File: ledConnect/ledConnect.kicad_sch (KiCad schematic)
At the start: 15 parts, among them U1 MT30-M, U2 TPS565208DDCR

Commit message: add layout
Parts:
- added Q1: AO4407A, easyeda2kicad:SOIC-8_L4.9-W3.9-P1.27-LS6.0-BL, symbol easyeda2kicad:AO4407A
- added R1: 100R, symbol Device:R
- added R2: 1M, symbol Device:R
- added SW1: SS-12M11G5, easyeda2kicad:SW-TH_XKB_SS-12M11XX, symbol easyeda2kicad:SS-12M11G5
- added TP4: LED_VDC, TestPoint:TestPoint_Pad_2.5x2.5mm, symbol Connector:TestPoint
- added TP5: LED_DATA, TestPoint:TestPoint_Pad_2.5x2.5mm, symbol Connector:TestPoint
- added TP6: LED_GND, TestPoint:TestPoint_Pad_2.5x2.5mm, symbol Connector:TestPoint
- TP1, TP2, TP3: footprint (none) -> TestPoint:TestPoint_Pad_2.5x2.5mm
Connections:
- net +12V: now also U1.3, Q1.5 (D), Q1.6 (D), Q1.7 (D), Q1.8 (D), R1.1; no longer C2.1, C3.1, C6.1, U2.3 (VIN), U2.5 (EN)
- net GND: now also TP1.1, U1.1, R2.2, TP6.1
- net LED_DATA: now also TP2.1, U1.2, TP5.1
- net VDC: now also TP3.1, SW1.3, TP4.1
- new net: Q1.4 (G), R1.2, R2.1
- new net: Q1.1 (S), Q1.2 (S), Q1.3 (S), SW1.1
- new net EN: C2.1, C3.1, C6.1, SW1.2, U2.3 (VIN), U2.5 (EN)
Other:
- note added: "reverse polarity protection"
- note added: "skip buck converter, if ledsignal is 5v anyway, or if the leds need 12v"
- moved on the sheet: C1, C2, C3, C4, C5, C6, C7, L1, Rfbb, Rfbt, TP1, TP2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

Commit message: next board
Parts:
- C2, C5, C6, C7: footprint (none) -> Capacitor_SMD:C_0805_2012Metric_Pad1.18x1.45mm_HandSolder
- C3, C4: footprint (none) -> Capacitor_SMD:C_0603_1608Metric_Pad1.08x0.95mm_HandSolder
- R1, R2: footprint (none) -> Resistor_SMD:R_0603_1608Metric_Pad0.98x0.95mm_HandSolder
- Rfbb1: renamed from Rfbb; footprint (none) -> Resistor_SMD:R_0603_1608Metric_Pad0.98x0.95mm_HandSolder
- Rfbt1: renamed from Rfbt; footprint (none) -> Resistor_SMD:R_0603_1608Metric_Pad0.98x0.95mm_HandSolder
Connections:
- net EN: now also SW1.1; no longer SW1.2
- net at Q1.1 (S), Q1.2 (S), Q1.3 (S): now also SW1.2; no longer SW1.1
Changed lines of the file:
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@@
 	(text "skip buck converter, \nif ledsignal is 5v anyway, \nor if the leds need 12v"
 		(exclude_from_sim no)
-		(at 108.458 59.69 0)
+		(at 113.03 52.832 0)
 		(effects
 			(font
@@
 	)
 	(junction
+		(at 119.38 73.66)
+		(diameter 0)
+		(color 0 0 0 0)
+	)
+	(junction
 		(at 171.45 81.28)
 		(diameter 0)
@@
 	)
 	(junction
-		(at 119.38 73.66)
-		(diameter 0)
-		(color 0 0 0 0)
-	)
-	(junction
 		(at 222.25 81.28)
 		(diameter 0)
@@
 	(wire
 		(pts
-			(xy 104.14 69.85) (xy 100.33 69.85)
-		)
-		(stroke
-			(width 0)
-			(type default)
-		)
-	)
-	(wire
-		(pts
 			(xy 170.18 129.54) (xy 168.91 129.54)
 		)
@@
 	(wire
 		(pts
-			(xy 95.25 69.85) (xy 95.25 71.12)
-		)
-		(stroke
-			(width 0)
-			(type default)
-		)
-	)
-	(wire
-		(pts
 			(xy 77.47 78.74) (xy 77.47 82.55)
 		)
@@
 	(wire
 		(pts
-			(xy 97.79 73.66) (xy 119.38 73.66)
-		)
-		(stroke
-			(width 0)
-			(type default)
-		)
-	)
-	(wire
-		(pts
 			(xy 119.38 81.28) (xy 132.08 81.28)
 		)
@@
 	(wire
 		(pts
-			(xy 95.25 71.12) (xy 85.09 71.12)
-		)
-		(stroke
-			(width 0)
-			(type default)
-		)
-	)
-	(wire
-		(pts
-			(xy 97.79 69.85) (xy 97.79 73.66)
+			(xy 85.09 71.12) (xy 97.79 71.12)
 		)
 		(stroke
@@
 	(wire
 		(pts
+			(xy 95.25 73.66) (xy 119.38 73.66)
+		)
+		(stroke
+			(width 0)
+			(type default)
+		)
+	)
+	(wire
+		(pts
 			(xy 204.47 74.93) (xy 204.47 81.28)
 		)
@@
 	(wire
 		(pts
+			(xy 95.25 69.85) (xy 95.25 73.66)
+		)
+		(stroke
+			(width 0)
+			(type default)
+		)
+	)
+	(wire
+		(pts
 			(xy 184.15 57.15) (xy 181.61 57.15)
 		)
@@
 		(pts
 			(xy 62.23 73.66) (xy 66.04 73.66)
+		)
+		(stroke
+			(width 0)
+			(type default)
+		)
+	)
+	(wire
+		(pts
+			(xy 97.79 71.12) (xy 97.79 69.85)
 		)
 		(stroke
@@
 			)
 		)
-		(property "Footprint" ""
+		(property "Footprint" "Resistor_SMD:R_0603_1608Metric_Pad0.98x0.95mm_HandSolder"
 			(at 64.262 87.63 90)
 			(effects
@@
 			)
 		)
-		(property "Footprint" ""
+		(property "Footprint" "Capacitor_SMD:C_0805_2012Metric_Pad1.18x1.45mm_HandSolder"
 			(at 235.9152 72.39 0)
 			(effects
@@
 			)
 		)
-		(property "Footprint" ""
+		(property "Footprint" "Capacitor_SMD:C_0805_2012Metric_Pad1.18x1.45mm_HandSolder"
 			(at 120.3452 81.28 0)
 			(effects
@@
 			)
 		)
-		(property "Footprint" ""
+		(property "Footprint" "Capacitor_SMD:C_0805_2012Metric_Pad1.18x1.45mm_HandSolder"
 			(at 223.2152 72.39 0)
 			(effects
@@
 			)
 		)
-		(property "Footprint" ""
+		(property "Footprint" "Capacitor_SMD:C_0603_1608Metric_Pad1.08x0.95mm_HandSolder"
 			(at 182.5752 64.77 0)
 			(effects
@@
 			)
 		)
-		(property "Footprint" ""
+		(property "Footprint" "Capacitor_SMD:C_0805_2012Metric_Pad1.18x1.45mm_HandSolder"
 			(at 133.0452 81.28 0)
 			(effects
@@
 	(symbol
 		(lib_id "power:VDC")
-		(at 104.14 69.85 270)
+		(at 100.33 69.85 270)
 		(unit 1)
 		(exclude_from_sim no)
@@
 		(fields_autoplaced yes)
 		(property "Reference" "#PWR012"
+			(at 96.52 69.85 0)
+			(effects
+				(font
+					(size 1.27 1.27)
+				)
+				(hide yes)
+			)
+		)
+		(property "Value" "VDC"
+			(at 104.14 69.8499 90)
+			(effects
+				(font
+					(size 1.27 1.27)
+				)
+				(justify left)
+			)
+		)
+		(property "Footprint" ""
 			(at 100.33 69.85 0)
 			(effects
@@
 			)
 		)
-		(property "Value" "VDC"
-			(at 107.95 69.8499 90)
-			(effects
-				(font
-					(size 1.27 1.27)
-				)
-				(justify left)
-			)
-		)
-		(property "Footprint" ""
-			(at 104.14 69.85 0)
-			(effects
-				(font
-					(size 1.27 1.27)
-				)
-				(hide yes)
-			)
-		)
 		(property "Datasheet" ""
-			(at 104.14 69.85 0)
+			(at 100.33 69.85 0)
 			(effects
 				(font
@@
 		)
 		(property "Description" "Power symbol creates a global label with name \"VDC\""
-			(at 104.14 69.85 0)
+			(at 100.33 69.85 0)
 			(effects
 				(font
@@
 			)
 		)
-		(property "Footprint" ""
+		(property "Footprint" "Resistor_SMD:R_0603_1608Metric_Pad0.98x0.95mm_HandSolder"
 			(at 64.262 77.47 90)
 			(effects
@@
 			)
 		)
-		(property "Footprint" ""
+		(property "Footprint" "Capacitor_SMD:C_0603_1608Metric_Pad1.08x0.95mm_HandSolder"
 			(at 145.7452 81.28 0)
 			(effects
@@
 		(dnp no)
 		(fields_autoplaced yes)
-		(property "Reference" "Rfbb"
+		(property "Reference" "Rfbb1"
 			(at 207.01 69.8499 0)
 			(effects
@@
 			)
 		)
-		(property "Footprint" ""
+		(property "Footprint" "Resistor_SMD:R_0603_1608Metric_Pad0.98x0.95mm_HandSolder"
 			(at 202.692 71.12 90)
 			(effects
@@
 			(project "ledConnect"
 				(path "/98174448-9966-40ca-80fa-f976aec9577e"
-					(reference "Rfbb")
+					(reference "Rfbb1")
 					(unit 1)
 				)
@@
 		(dnp no)
 		(fields_autoplaced yes)
-		(property "Reference" "Rfbt"
+		(property "Reference" "Rfbt1"
 			(at 207.01 59.6899 0)
 			(effects
@@
 			)
 		)
-		(property "Footprint" ""
+		(property "Footprint" "Resistor_SMD:R_0603_1608Metric_Pad0.98x0.95mm_HandSolder"
 			(at 202.692 60.96 90)
 			(effects
@@
 			(project ""
 				(path "/98174448-9966-40ca-80fa-f976aec9577e"
-					(reference "Rfbt")
-					(unit 1)
-				)
+					(reference "Rfbt1")
+					(unit 1)
+				)

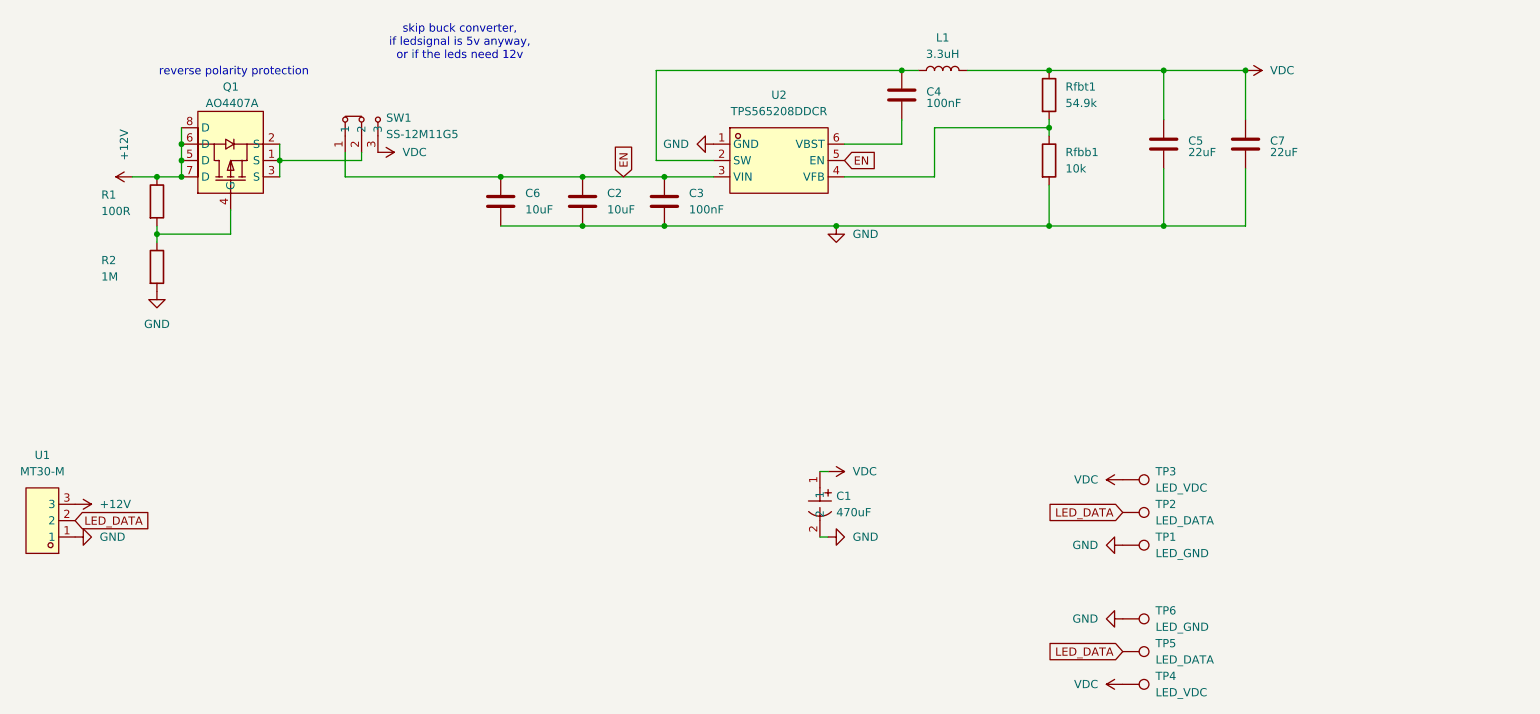
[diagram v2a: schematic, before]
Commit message: via stiching fehlt noch
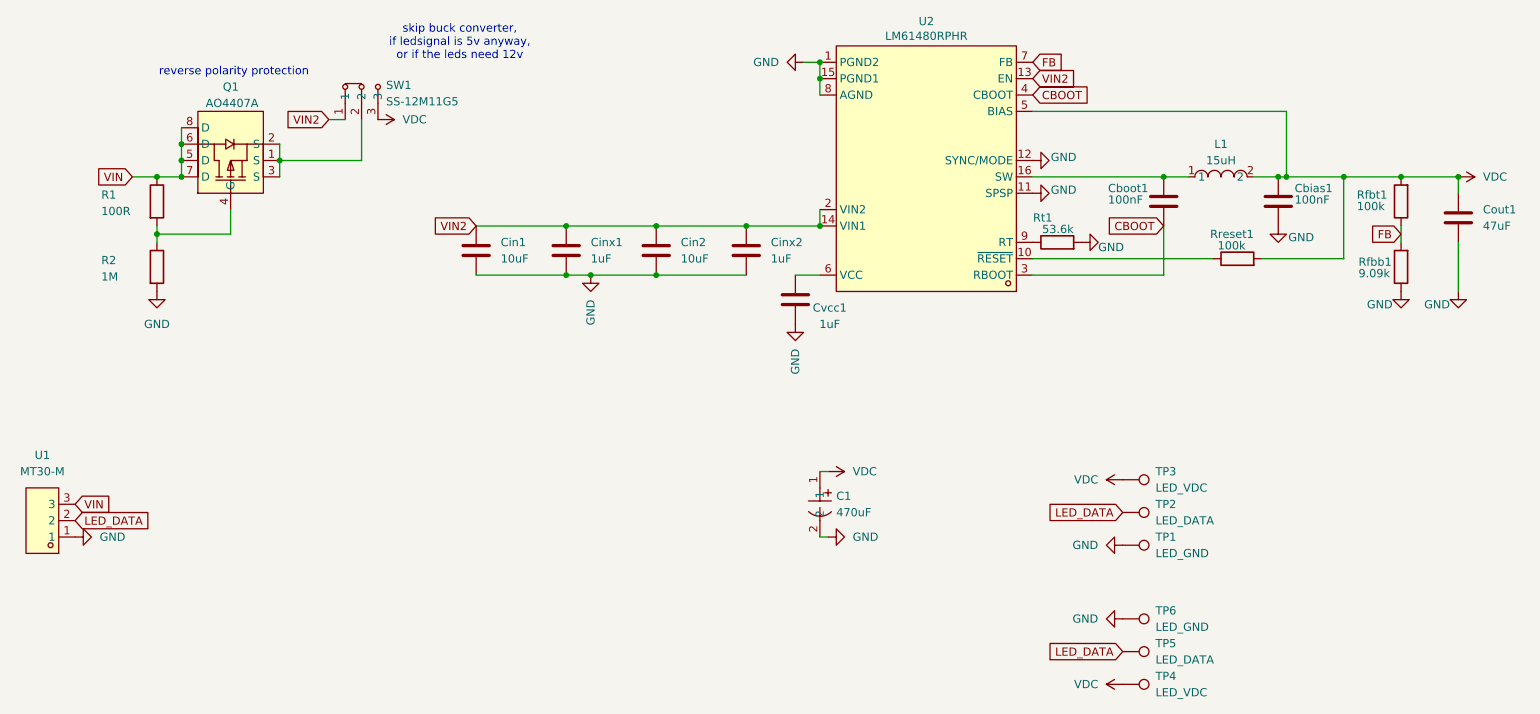
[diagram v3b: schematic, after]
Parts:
- removed C2, C6: 10uF, Capacitor_SMD:C_0805_2012Metric_Pad1.18x1.45mm_HandSolder, symbol Device:C
- removed C3, C4: 100nF, Capacitor_SMD:C_0603_1608Metric_Pad1.08x0.95mm_HandSolder, symbol Device:C
- removed C5, C7: 22uF, Capacitor_SMD:C_0805_2012Metric_Pad1.18x1.45mm_HandSolder, symbol Device:C
- removed L1: 3.3uH, Inductor_SMD:L_TaiTech_TMPC1265_13.5x12.5mm, symbol Device:L
- removed U2: TPS565208DDCR, easyeda2kicad:TSOT-23-6_L2.9-W1.6-P0.95-LS2.8-BR, symbol easyeda2kicad:TPS565208DDCR
- added Cbias1: 100nF, symbol Device:C
- added Cboot1: 100nF, Capacitor_SMD:C_0603_1608Metric_Pad1.08x0.95mm_HandSolder, symbol Device:C
- added Cin1, Cin2: 10uF, Capacitor_SMD:C_0603_1608Metric_Pad1.08x0.95mm_HandSolder, symbol Device:C
- added Cinx1, Cinx2, Cvcc1: 1uF, Capacitor_SMD:C_0603_1608Metric_Pad1.08x0.95mm_HandSolder, symbol Device:C
- added Cout1: 47uF, Capacitor_SMD:C_1210_3225Metric_Pad1.33x2.70mm_HandSolder, symbol Device:C
- added L1: 15uH, easyeda2kicad:IND-SMD_L13.5-W12.6, symbol easyeda2kicad:MDA1350-150M
- added Rreset1: 100k, Resistor_SMD:R_0603_1608Metric_Pad0.98x0.95mm_HandSolder, symbol Device:R
- added Rt1: 53.6k, Resistor_SMD:R_0603_1608Metric_Pad0.98x0.95mm_HandSolder, symbol Device:R
- added U2: LM61480RPHR, easyeda2kicad:VQFN-16_L4.5-W3.5-P0.50-TL_TI_RPH, symbol easyeda2kicad:LM61480RPHR
- Rfbb1: value 10k -> 9.09k
- Rfbt1: value 54.9k -> 100k
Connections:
- net GND: now also Rfbb1.1, Cbias1.2, Cin1.2, Cin2.2, Cinx1.2, Cinx2.2, Cout1.2, Cvcc1.2, Rt1.2, U2.1 (PGND2), U2.11 (SPSP), U2.12 (SYNC/MODE), U2.15 (PGND1), U2.8 (AGND); no longer Rfbb1.2
- net VDC: now also Rfbt1.2, Cbias1.1, Cout1.1, L1.2, Rreset1.2, U2.5 (BIAS); no longer Rfbt1.1
- net +12V renamed VIN
- net EN renamed VIN2
- net VIN2: now also Cin1.1, Cin2.1, Cinx1.1, Cinx2.1, U2.13 (EN), U2.14 (VIN1), U2.2 (VIN2)
- new net: Rreset1.1, U2.10 (~{RESET})
- new net: Cboot1.1, L1.1, U2.16 (SW)
- new net: Cvcc1.1, U2.6 (VCC)
- new net: Rt1.1, U2.9 (RT)
- new net CBOOT: Cboot1.2, U2.3 (RBOOT), U2.4 (CBOOT)
- new net FB: Rfbb1.2, Rfbt1.1, U2.7 (FB)
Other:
- moved on the sheet: SW1

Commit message: update
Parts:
- U2: value LM61480RPHR -> LM61495RPHR
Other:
- note added: "L1 12V version: 15uH 5V version: 3.3uH"
- note added: "Rfbb1 12V version: 9.09k 5V version: 24.9k"
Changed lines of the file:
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@@
+		)
+	)
+	(text "Rfbb1\n12V version: 9.09k\n5V version: 24.9k"
+		(exclude_from_sim no)
+		(at 244.856 91.694 0)
+		(effects
+			(font
+				(size 1.27 1.27)
+			)
+		)
+	)
+	(text "L1\n12V version: 15uH\n5V version: 3.3uH"
+		(exclude_from_sim no)
+		(at 219.964 68.072 0)
+		(effects
+			(font
+				(size 1.27 1.27)
+			)
 		)
 	)
@@
 			)
 		)
-		(property "Value" "LM61480RPHR"
+		(property "Value" "LM61495RPHR"
 			(at 185.42 51.816 0)
 			(effects
